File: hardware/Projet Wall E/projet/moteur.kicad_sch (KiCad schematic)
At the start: 9 parts, among them J4 Conn_01x06, J5 Conn_01x06, U5 DRV8833PWP

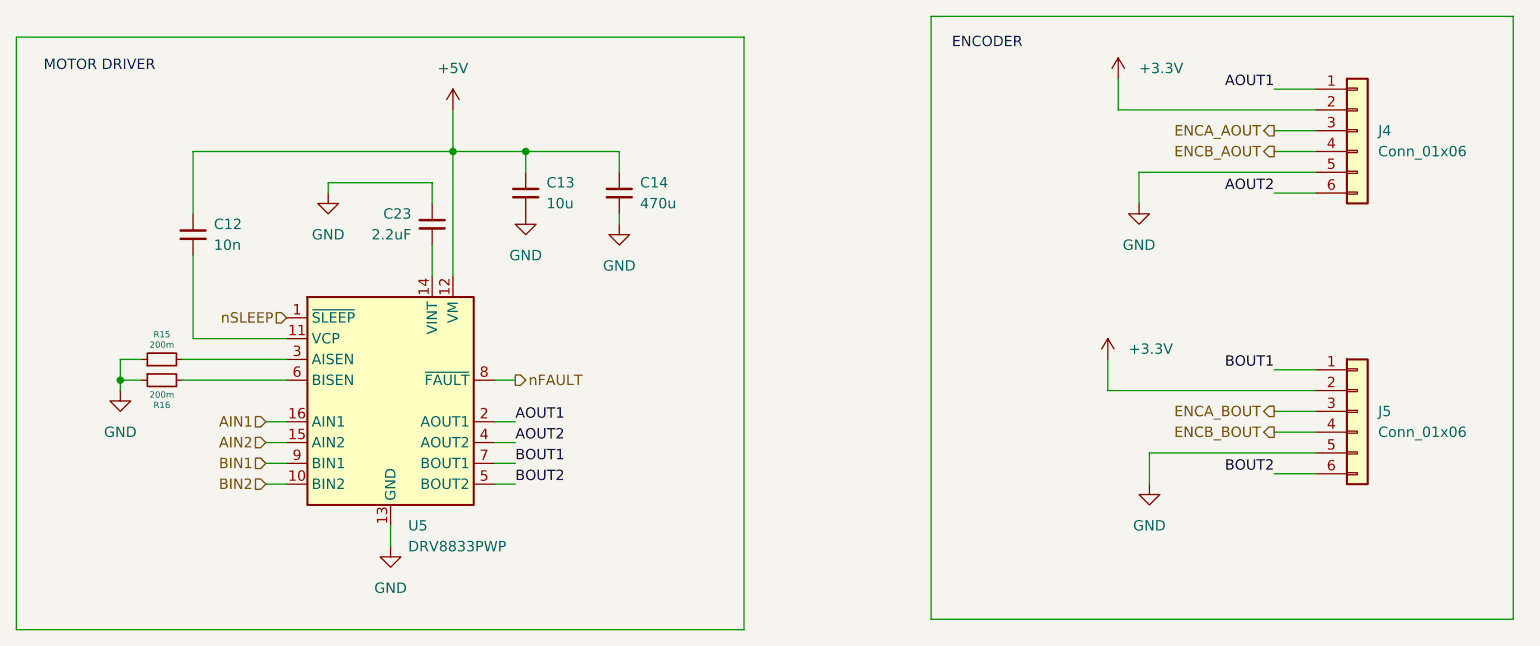
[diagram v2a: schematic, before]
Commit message: Intégration du schéma moteur de feature-puissance
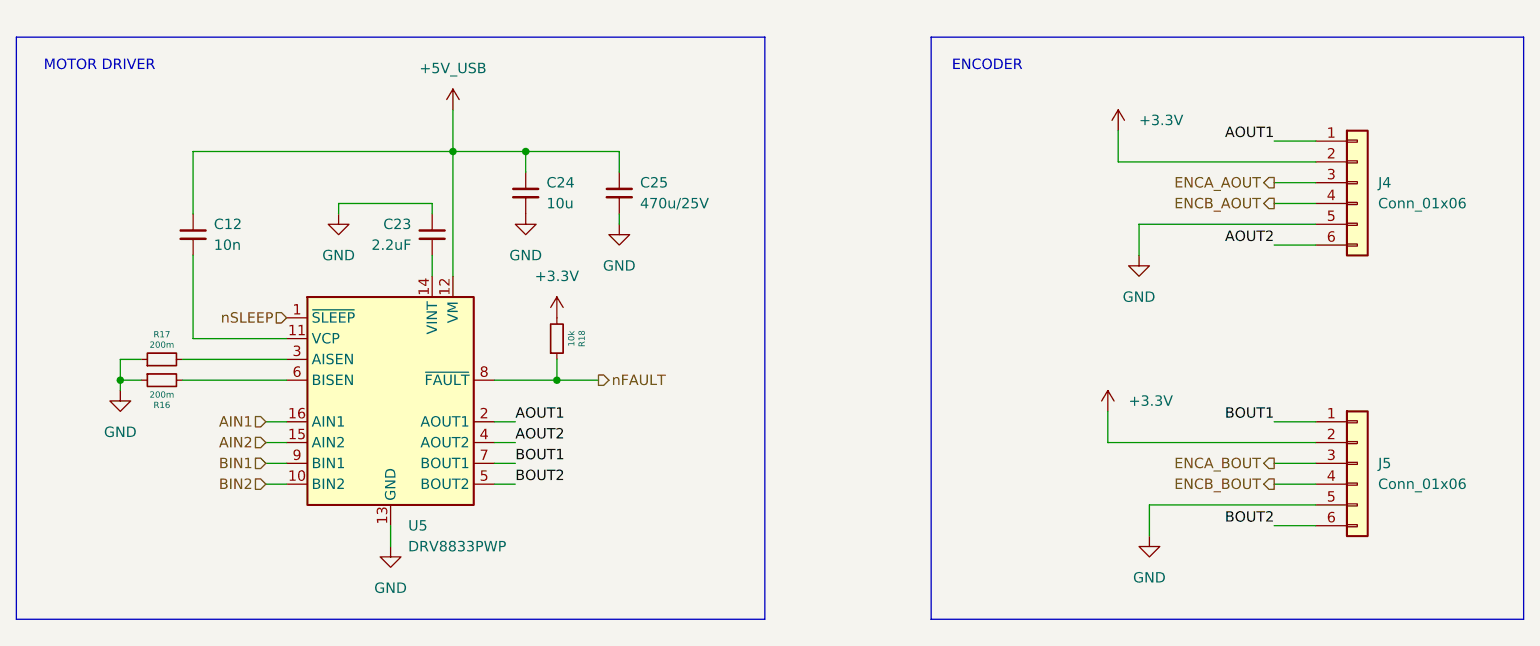
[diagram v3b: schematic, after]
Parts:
- removed C13: 10u, Capacitor_SMD:C_01005_0402Metric, symbol Device:C_Small
- removed C14: 470u, Capacitor_SMD:C_01005_0402Metric, symbol Device:C_Small
- removed R15: 200m, Resistor_SMD:R_0201_0603Metric, symbol Device:R_Small
- added C24: 10u, Capacitor_SMD:C_01005_0402Metric, symbol Device:C_Small
- added C25: 470u/25V, Capacitor_SMD:C_01005_0402Metric, symbol Device:C_Small
- added R17: 200m, Resistor_SMD:R_0201_0603Metric, symbol Device:R_Small
- added R18: 10k, Resistor_SMD:R_0201_0603Metric, symbol Device:R_Small
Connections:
- net +3.3V: now also R18.2
- net GND: now also C24.2, C25.2, R17.1
- net nFAULT: now also R18.1
- net at U5.3 (AISEN): now also R17.2
- net +5V renamed +5V_USB
- net +5V_USB: now also C24.1, C25.1
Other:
- moved on the sheet: C23, J4, J5

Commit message: feat: mise a jour alim reference jlcpcb
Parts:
- U5: JLCPCB Part # (none) -> C1556089
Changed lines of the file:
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@@
+			)
+		)
+		(property "JLCPCB Part #" "C1556089"
+			(at 85.09 82.55 0)
+			(hide yes)
+			(show_name no)
+			(do_not_autoplace no)
+			(effects
+				(font
+					(size 1.27 1.27)
+				)
 			)
 		)
